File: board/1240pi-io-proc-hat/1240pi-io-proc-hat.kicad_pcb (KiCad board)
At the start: 2 copper layers, 29.2 x 63.5 mm, 12 parts, among them J1 62684-50210, J2 SFV10R-1ST, P445 Header, U445 Z80

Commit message: Add description to IO proc interface.
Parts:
- removed R2, R3, R4, R6: 10k, Resistor_SMD:R_0805_2012Metric
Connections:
- P445 pad 18: unconnected-(P445-Pad18) -> /~{HALT}
- P445 pad 20: unconnected-(P445-Pad20) -> /~{IORQ}
- P445 pad 23: unconnected-(P445-Pad23) -> /~{BUSACK}
- P445 pad 28: unconnected-(P445-Pad28) -> /~{RFSH}
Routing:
- net +5V: track 53.3 -> 48.2 mm
- net /~{MREQ}: track 29.6 -> 25.8 mm
- net /D1: track 28.6 -> 27.0 mm
- net /~{RFSH}: track 40.1 -> 38.7 mm
- net /~{BUSACK}: track 19.3 -> 17.9 mm
- net /~{HALT}: track 28.8 -> 29.8 mm
- net /~{IORQ}: track 29.5 -> 30.4 mm

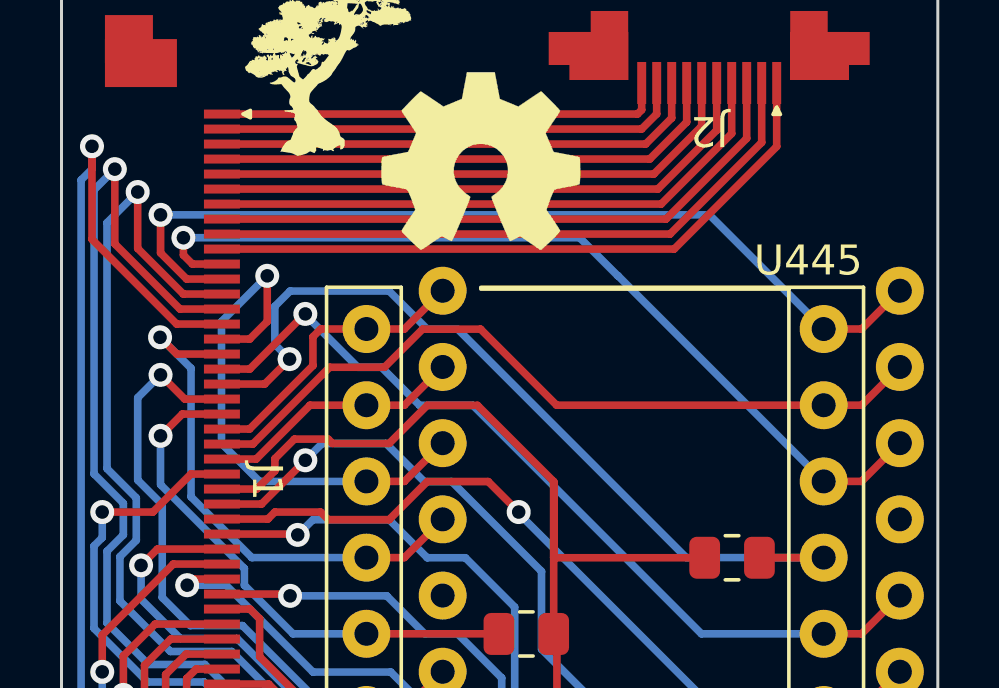
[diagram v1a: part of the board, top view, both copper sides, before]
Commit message: Reroute IO Proc hat again and add buffers on rompack board.
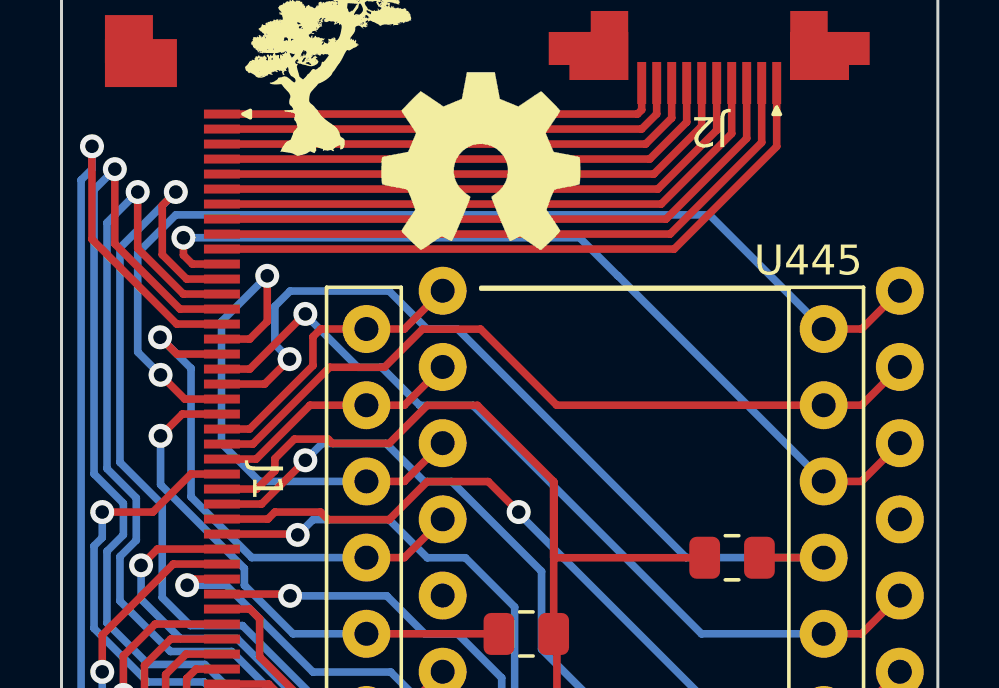
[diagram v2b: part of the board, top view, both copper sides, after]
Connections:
- J1 pad 12: /~{IORQ} -> /~{RESET}
- J1 pad 20: /~{RESET} -> /~{IORQ}
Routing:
- net /~{RESET}: track 21.9 -> 30.9 mm
- net /~{IORQ}: track 30.4 -> 34.8 mm
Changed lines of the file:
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@@
       (net 35 "/~{HALT}") (pinfunction "Pin_11") (pintype "passive"))
     (pad "12" smd rect locked (at -6.75 -2.3 270) (size 0.3 1.2) (layers "F.Cu" "F.Paste" "F.Mask")
-      (net 36 "/~{IORQ}") (pinfunction "Pin_12") (pintype "passive"))
+      (net 26 "/~{RESET}") (pinfunction "Pin_12") (pintype "passive"))
     (pad "13" smd rect locked (at -6.25 -2.3 270) (size 0.3 1.2) (layers "F.Cu" "F.Paste" "F.Mask")
       (net 38 "/~{M1}") (pinfunction "Pin_13") (pintype "passive"))
@@
       (net 34 "/~{NMI}") (pinfunction "Pin_19") (pintype "passive"))
     (pad "20" smd rect locked (at -2.75 -2.3 270) (size 0.3 1.2) (layers "F.Cu" "F.Paste" "F.Mask")
-      (net 26 "/~{RESET}") (pinfunction "Pin_20") (pintype "passive"))
+      (net 36 "/~{IORQ}") (pinfunction "Pin_20") (pintype "passive"))
     (pad "21" smd rect locked (at -2.25 -2.3 270) (size 0.3 1.2) (layers "F.Cu" "F.Paste" "F.Mask")
       (net 46 "/~{BUSREQ}") (pinfunction "Pin_21") (pintype "passive"))
@@
   (segment (start 145.439212 57.15) (end 146.709212 58.42) (width 0.254) (layer "B.Cu") (net 25))
   (segment (start 144.785 66.035) (end 146.05 66.035) (width 0.254) (layer "F.Cu") (net 26))
-  (segment (start 138.728 55.67) (end 137.922 54.864) (width 0.254) (layer "F.Cu") (net 26))
-  (segment (start 139.968 55.67) (end 138.728 55.67) (width 0.254) (layer "F.Cu") (net 26))
+  (segment (start 138.792 51.67) (end 139.968 51.67) (width 0.254) (layer "F.Cu") (net 26))
+  (segment (start 137.9792 50.8572) (end 138.792 51.67) (width 0.254) (layer "F.Cu") (net 26))
+  (segment (start 138.43 48.768) (end 137.9792 49.2188) (width 0.254) (layer "F.Cu") (net 26))
+  (segment (start 137.9792 49.2188) (end 137.9792 50.8572) (width 0.254) (layer "F.Cu") (net 26))
   (segment (start 146.05 66.035) (end 147.325 64.76) (width 0.254) (layer "F.Cu") (net 26))
-  (via (at 137.922 54.864) (size 0.8) (drill 0.45) (layers "F.Cu" "B.Cu") (net 26))
+  (via (at 138.43 48.768) (size 0.8) (drill 0.45) (layers "F.Cu" "B.Cu") (net 26))
+  (segment (start 144.785 66.035) (end 143.466316 66.035) (width 0.254) (layer "B.Cu") (net 26))
   (segment (start 140.651916 63.2206) (end 138.9126 63.2206) (width 0.254) (layer "B.Cu") (net 26))
-  (segment (start 137.977669 59.188985) (end 137.16 58.371316) (width 0.254) (layer "B.Cu") (net 26))
   (segment (start 143.466316 66.035) (end 140.651916 63.2206) (width 0.254) (layer "B.Cu") (net 26))
-  (segment (start 137.16 55.626) (end 137.922 54.864) (width 0.254) (layer "B.Cu") (net 26))
-  (segment (start 137.16 58.371316) (end 137.16 55.626) (width 0.254) (layer "B.Cu") (net 26))
-  (segment (start 144.785 66.035) (end 143.466316 66.035) (width 0.254) (layer "B.Cu") (net 26))
   (segment (start 138.9126 63.2206) (end 137.977669 62.285669) (width 0.254) (layer "B.Cu") (net 26))
   (segment (start 137.977669 62.285669) (end 137.977669 59.188985) (width 0.254) (layer "B.Cu") (net 26))
+  (segment (start 136.568569 57.779885) (end 136.568569 50.629431) (width 0.254) (layer "B.Cu") (net 26))
+  (segment (start 136.568569 50.629431) (end 138.43 48.768) (width 0.254) (layer "B.Cu") (net 26))
+  (segment (start 137.977669 59.188985) (end 136.568569 57.779885) (width 0.254) (layer "B.Cu") (net 26))
   (segment (start 148.844 58.42) (end 146.812 58.42) (width 0.254) (layer "F.Cu") (net 27))
   (segment (start 160.025 66.035) (end 161.29 66.035) (width 0.254) (layer "F.Cu") (net 27))
@@
   (segment (start 151.892 50.292) (end 138.684 50.292) (width 0.254) (layer "B.Cu") (net 35))
   (segment (start 153.172 51.562) (end 153.162 51.562) (width 0.254) (layer "B.Cu") (net 35))
-  (segment (start 138.792 51.67) (end 139.968 51.67) (width 0.254) (layer "F.Cu") (net 36))
-  (segment (start 137.922 49.53) (end 137.922 50.8) (width 0.254) (layer "F.Cu") (net 36))
-  (segment (start 137.922 50.8) (end 138.792 51.67) (width 0.254) (layer "F.Cu") (net 36))
+  (segment (start 138.728 55.67) (end 137.922 54.864) (width 0.254) (layer "F.Cu") (net 36))
+  (segment (start 139.968 55.67) (end 138.728 55.67) (width 0.254) (layer "F.Cu") (net 36))
   (segment (start 161.29 53.335) (end 162.565 52.06) (width 0.254) (layer "F.Cu") (net 36))
   (segment (start 160.025 53.335) (end 161.29 53.335) (width 0.254) (layer "F.Cu") (net 36))
-  (via (at 137.922 49.53) (size 0.8) (drill 0.45) (layers "F.Cu" "B.Cu") (net 36))
-  (segment (start 160.025 53.335) (end 156.22 49.53) (width 0.254) (layer "B.Cu") (net 36))
-  (segment (start 156.22 49.53) (end 137.922 49.53) (width 0.254) (layer "B.Cu") (net 36))
+  (via (at 137.922 54.864) (size 0.8) (drill 0.45) (layers "F.Cu" "B.Cu") (net 36))
+  (segment (start 156.22 49.53) (end 160.025 53.335) (width 0.254) (layer "B.Cu") (net 36))
+  (segment (start 138.43 49.53) (end 156.22 49.53) (width 0.254) (layer "B.Cu") (net 36))
+  (segment (start 137.16 54.102) (end 137.16 50.8) (width 0.254) (layer "B.Cu") (net 36))
+  (segment (start 137.16 50.8) (end 138.43 49.53) (width 0.254) (layer "B.Cu") (net 36))
+  (segment (start 137.922 54.864) (end 137.16 54.102) (width 0.254) (layer "B.Cu") (net 36))
   (segment (start 140.894 53.67) (end 141.478 53.086) (width 0.254) (layer "F.Cu") (net 37))
   (segment (start 144.785 58.415) (end 146.05 58.415) (width 0.254) (layer "F.Cu") (net 37))
